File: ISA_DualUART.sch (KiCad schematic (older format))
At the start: 75 parts, among them J1 ISA BUS, J10 Parallel Port, J2 ADDR_IRQ, J3 UART1_SEL, J4 UART2_SEL, J6 Serial 2 IDC, J7 Serial 1 DB9, J9 Parport IRQ Select, U1 74LS138, U11 74LS30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

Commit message: Reworked the board, added LED indicators for parport
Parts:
- removed R10, R11, R12, R13, R14, R15, R16, R9: 4.7k, Resistor_THT:R_Axial_DIN0207_L6.3mm_D2.5mm_P10.16mm_Horizontal, symbol Device:R_Small
- added J5: Parallel Port LEDs, Package_DIP:DIP-20_W7.62mm_Socket_LongPads, symbol Connector_Generic:Conn_02x10_Counter_Clockwise
- added RN1: 4.7k, Resistor_THT:R_Array_SIP9, symbol Device:R_Network08
- added RN2: 1k, Resistor_THT:R_Array_SIP11, symbol Device:R_Network10
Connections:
- net GND: now also RN2.1 (common)
- net PARPORT_DATA0: now also J5.8 (Pin_8)
- net PARPORT_DATA1: now also J5.7 (Pin_7)
- net PARPORT_DATA2: now also J5.6 (Pin_6)
- net PARPORT_DATA3: now also J5.5 (Pin_5)
- net PARPORT_DATA4: now also J5.4 (Pin_4)
- net PARPORT_DATA5: now also J5.3 (Pin_3)
- net PARPORT_DATA6: now also J5.2 (Pin_2)
- net PARPORT_DATA7: now also J5.1 (Pin_1)
- net VCC: now also RN1.1 (common)
- net RN_1: now reaches JP1.2, U12.4
- net RN_1: now also RN1.2 (R1)
- net RN_3: now reaches U18.11, U18.4
- net RN_3: now also RN1.4 (R3)
- net RN_8: now reaches U18.12, U20.13 (I1b)
- net RN_8: now also RN1.9 (R8)
- net ~PARPORT_ACK renamed RN_7
- net RN_7: now also J5.9 (Pin_9), RN1.8 (R7)
- net ~PARPORT_AUTOFD renamed RN_5
- net RN_5: now also RN1.6 (R5)
- net ~PARPORT_INIT renamed RN_4
- net RN_4: now also RN1.5 (R4)
- net ~PARPORT_SLCTIN renamed RN_2
- net RN_2: now also RN1.3 (R2)
- net ~PARPORT_STROBE renamed RN_6
- net RN_6: now also J5.10 (Pin_10), RN1.7 (R6)
- new net: J5.12 (Pin_12), RN2.10 (R9)
- new net: J5.11 (Pin_11), RN2.11 (R10)
- new net: J5.20 (Pin_20), RN2.2 (R1)
- new net: J5.19 (Pin_19), RN2.3 (R2)
- new net: J5.18 (Pin_18), RN2.4 (R3)
- new net: J5.17 (Pin_17), RN2.5 (R4)
- new net: J5.16 (Pin_16), RN2.6 (R5)
- new net: J5.15 (Pin_15), RN2.7 (R6)
- new net: J5.14 (Pin_14), RN2.8 (R7)
- new net: J5.13 (Pin_13), RN2.9 (R8)

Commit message: Updated schematics
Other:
- note added: "Open - 0x278/9/A\nClosed - 0x378/9/A"
- note removed: "Closed - 0x278/9/A\nOpen - 0x378/9/A"
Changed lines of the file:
@@
 	6400 6450 6650 6450
 Text Notes 5350 7150 0    50   ~ 0
-Closed - 0x278/9/A\nOpen    - 0x378/9/A
+Open - 0x278/9/A\nClosed - 0x378/9/A
 $Comp
 L 74xx:74LS02 U13

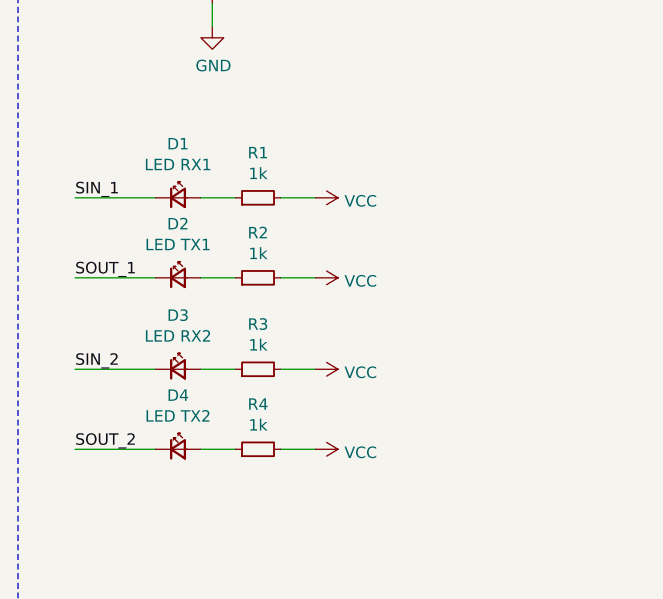
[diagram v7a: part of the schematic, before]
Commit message: Slight changes to silkscreen
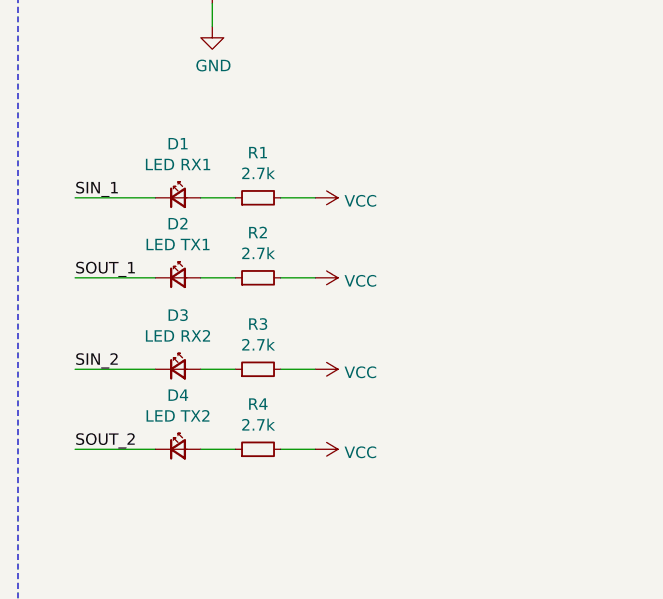
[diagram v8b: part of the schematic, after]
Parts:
- R1, R2, R3, R4: value 1k -> 2.7k
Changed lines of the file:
@@
 P 1800 2700
 F 0 "R1" V 1996 2700 50  0000 C CNN
-F 1 "1k" V 1905 2700 50  0000 C CNN
+F 1 "2.7k" V 1905 2700 50  0000 C CNN
 F 2 "Resistor_THT:R_Axial_DIN0207_L6.3mm_D2.5mm_P10.16mm_Horizontal" H 1800 2700 50  0001 C CNN
 F 3 "~" H 1800 2700 50  0001 C CNN
@@
 P 1800 3050
 F 0 "R2" V 1996 3050 50  0000 C CNN
-F 1 "1k" V 1905 3050 50  0000 C CNN
+F 1 "2.7k" V 1905 3050 50  0000 C CNN
 F 2 "Resistor_THT:R_Axial_DIN0207_L6.3mm_D2.5mm_P10.16mm_Horizontal" H 1800 3050 50  0001 C CNN
 F 3 "~" H 1800 3050 50  0001 C CNN
@@
 P 1800 3450
 F 0 "R3" V 1996 3450 50  0000 C CNN
-F 1 "1k" V 1905 3450 50  0000 C CNN
+F 1 "2.7k" V 1905 3450 50  0000 C CNN
 F 2 "Resistor_THT:R_Axial_DIN0207_L6.3mm_D2.5mm_P10.16mm_Horizontal" H 1800 3450 50  0001 C CNN
 F 3 "~" H 1800 3450 50  0001 C CNN
@@
 P 1800 3800
 F 0 "R4" V 1996 3800 50  0000 C CNN
-F 1 "1k" V 1905 3800 50  0000 C CNN
+F 1 "2.7k" V 1905 3800 50  0000 C CNN
 F 2 "Resistor_THT:R_Axial_DIN0207_L6.3mm_D2.5mm_P10.16mm_Horizontal" H 1800 3800 50  0001 C CNN
 F 3 "~" H 1800 3800 50  0001 C CNN
